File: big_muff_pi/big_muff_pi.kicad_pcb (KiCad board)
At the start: 2 copper layers, 80 x 100 mm, 77 parts, among them J1 Jack_6.35, J2 Jack_6.35, J3 Conn_01x05, J4 Conn_01x05, J5 Conn_01x05, J7 Conn_01x01_Socket, J8 Conn_01x01_Socket, J9 Barrel_Jack_Switch, P1 big_muff_pi_front_panel, Q1 MMBT5551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

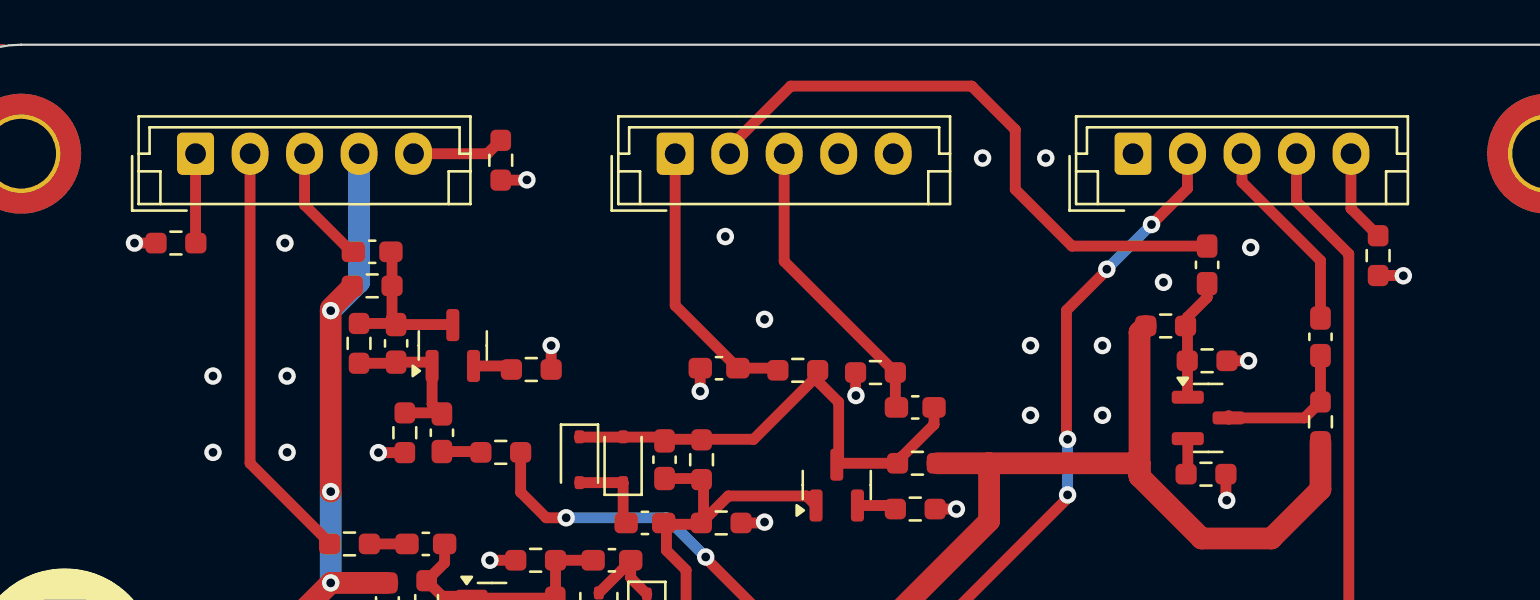
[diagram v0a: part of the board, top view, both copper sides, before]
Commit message: Added IDC, added front plate.
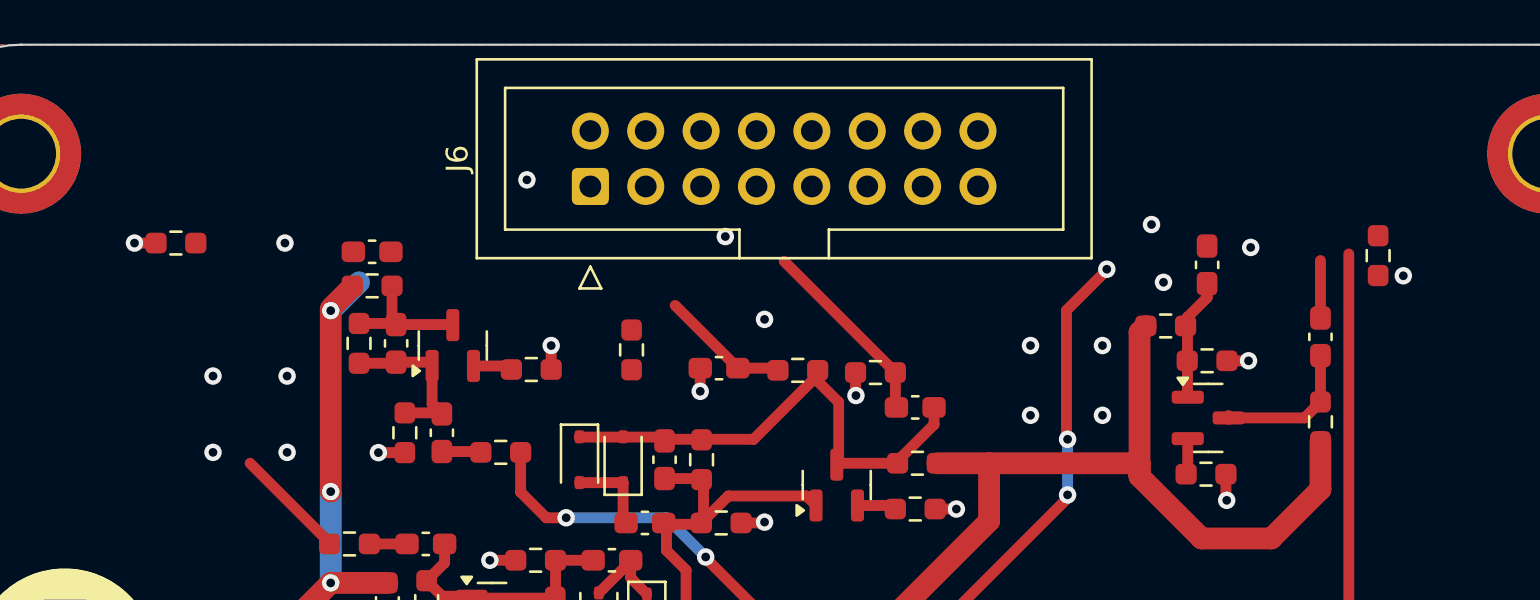
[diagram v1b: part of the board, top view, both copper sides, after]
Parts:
- removed J3, J4, J5: Conn_01x05, Connector_JST:JST_EH_B5B-EH-A_1x05_P2.50mm_Vertical
- added J6: top_panel_connector, Connector_IDC:IDC-Header_2x08_P2.54mm_Vertical, F.Cu at (81.1, 56.5)
- moved R25 10.6 mm to (83.0, 64.0)
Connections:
- R25 pad 1: Net-(J3-Pin_5) -> 9V
- R25 pad 2: 0 -> Net-(J6E-Pin_10)
- R26 pad 2: 0 -> Net-(SW1B-B)
- SW1 pad 5: Net-(J5-Pin_4) -> Net-(SW1B-B)
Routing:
- net Net-(J5-Pin_4): track 100.1 -> 0.00 mm, vias 2 -> 0
- net Net-(SW1B-B): track 0.00 -> 94.5 mm, vias 0 -> 2
- net F_OUT: track 28.0 -> 0.00 mm
- net Net-(J6A-Pin_4): track 19.4 -> 5.21 mm
- net Net-(J6B-Pin_9): track 12.9 -> 5.94 mm
- net Net-(J6C-Pin_14): track 70.5 -> 63.6 mm
- net Net-(J6C-Pin_12): track 9.03 -> 2.64 mm
- net 9V: track 220.5 -> 214.6 mm
- net FS_OUT: track 5.48 -> 0.00 mm
- net Net-(J6B-Pin_5): track 13.8 -> 8.83 mm
- net Net-(J6D-Pin_8): track 4.28 -> 0.00 mm
- net Net-(J3-Pin_5): track 4.25 -> 0.00 mm
- net Net-(J6A-Pin_6): track 4.11 -> 0.00 mm
- net 0: track 18.9 -> 16.5 mm, vias 60 -> 58
- net Net-(Q4-C): track 7.65 -> 6.07 mm

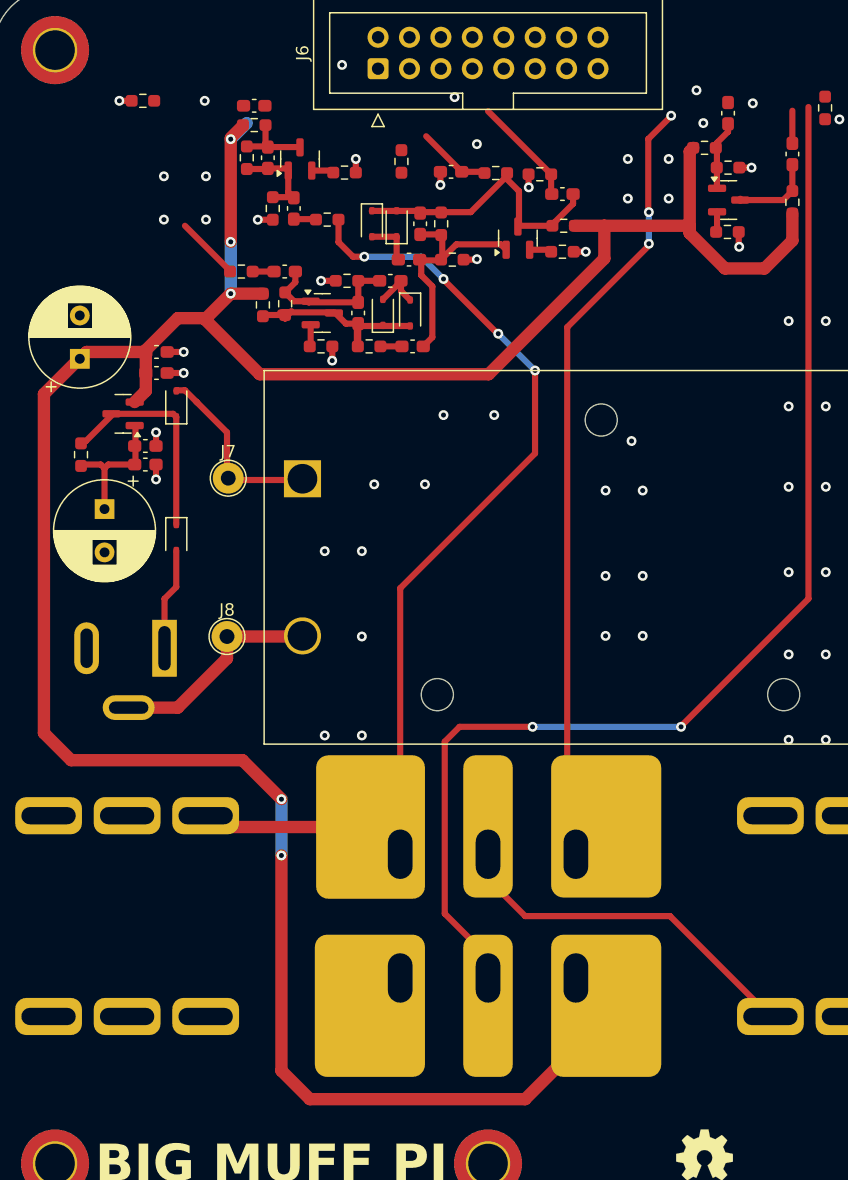
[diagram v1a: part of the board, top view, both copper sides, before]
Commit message: Inputs rotated, power conn moved, spacers updated.
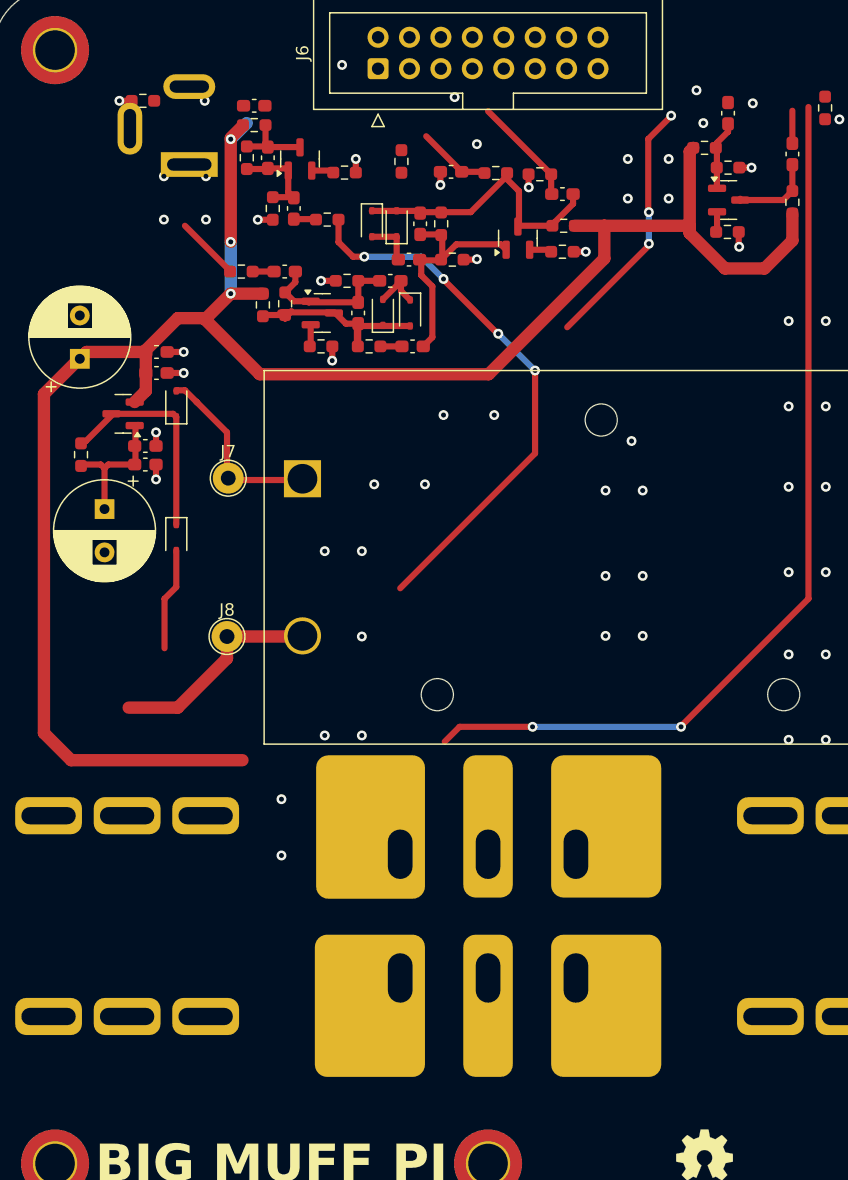
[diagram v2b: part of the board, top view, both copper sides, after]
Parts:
- moved J1 48.4 mm to (112.8, 116.9), turned to 0 degrees
- moved J2 48.4 mm to (67.2, 133.1), turned to 180 degrees
- moved J9 39.2 mm to (65.8, 64.2), turned to 180 degrees
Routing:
- net 9V: track 214.6 -> 156.0 mm
- net Net-(J6C-Pin_14): track 63.6 -> 20.7 mm
- net SW_IN: track 82.7 -> 44.2 mm
- net Net-(SW1A-B): track 29.4 -> 0.00 mm
- net Net-(SW1B-B): track 94.5 -> 74.0 mm

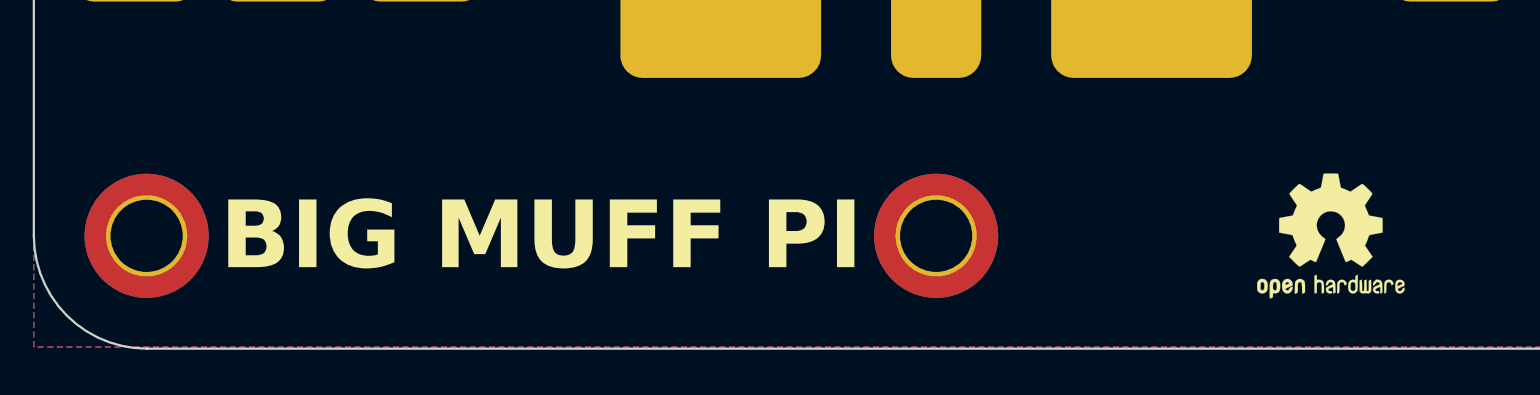
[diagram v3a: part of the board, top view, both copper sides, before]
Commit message: Potentiometers checked, LED updated
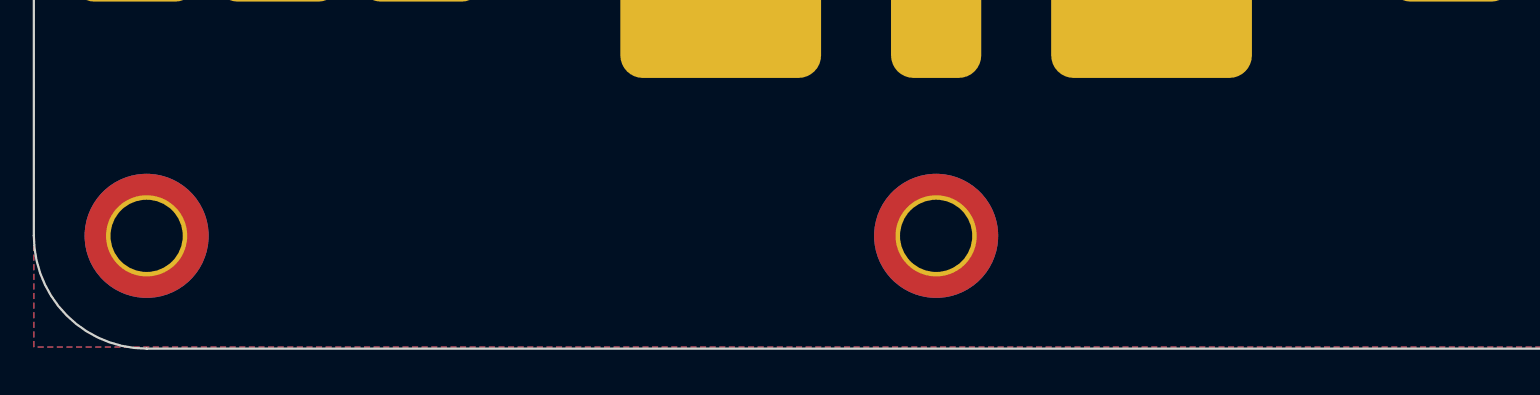
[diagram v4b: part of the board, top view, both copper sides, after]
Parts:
- added REF**: TI logo, pedale:TI logo, B.Cu at (115.5, 145.0)
- SIM1: moved to B.Cu
- moved SIM1 0.25 mm to (107.2, 145.0), turned to 180 degrees
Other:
- board text added: "BMF"
- board text added: "ostojaatanasijevic"
- board text removed: "BIG MUFF PI"

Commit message: small work
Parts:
- removed D4, D7: 1N4148WS, Diode_SMD:D_SOD-323
- removed REF**: TI logo, pedale:TI logo
- added P2: bottom_panel, pedale:bottom_plate, F.Cu at (50.0, 50.0)
- added Q10: AO3401A, Package_TO_SOT_SMD:SOT-23, F.Cu at (60.1, 68.0)
- added Q12: AO3400A, Package_TO_SOT_SMD:SOT-23, F.Cu at (20.5, 72.0)
- added Q13: AO3400A, Package_TO_SOT_SMD:SOT-23, F.Cu at (56.1, 71.5)
- added Q14: AO3400A, Package_TO_SOT_SMD:SOT-23, F.Cu at (56.1, 68.0)
- added Q6: AO3401A, Package_TO_SOT_SMD:SOT-23, F.Cu at (20.5, 58.1)
- added Q8: AO3401A, Package_TO_SOT_SMD:SOT-23, F.Cu at (60.1, 71.5)
- added R23: 100k, Resistor_SMD:R_0603_1608Metric_Pad0.98x0.95mm_HandSolder, F.Cu at (25.1, 57.0)
- added R27: 100k, Resistor_SMD:R_0603_1608Metric_Pad0.98x0.95mm_HandSolder, F.Cu at (25.1, 59.5)
- moved C14 77.6 mm to (-11.2, 112.0)
- moved C16 77.6 mm to (-10.3, 106.1)
- moved C17 77.6 mm to (-10.3, 104.4)
- moved C18 77.6 mm to (-11.2, 113.5)
- moved C19 77.6 mm to (-16.5, 105.0)
- moved C20 77.6 mm to (-14.5, 117.1)
- moved Q5 77.6 mm to (-13.0, 109.4)
- moved R24 77.6 mm to (-16.4, 112.7)
- moved R6 14.0 mm to (73.8, 51.5)
- moved BT1 4.45 mm to (75.0, 94.1)
- moved J7 4.40 mm to (69.0, 94.0)
- moved J8 4.40 mm to (68.9, 106.8)
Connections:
- net Net-(BT1-+) renamed BAT+
- net Net-(BT1--) renamed BAT-
- net Net-(D4-K) renamed REG_IN
- J1 pad SN: unconnected-(J1-PadSN) -> IN_CONNECT
- J9 pad 1: Net-(D7-A) -> CONN+
- J9 pad 2: 0 -> CONN-
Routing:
- net Net-(SW1B-B): track 74.0 -> 0.00 mm
- net 9V: track 156.0 -> 111.7 mm
- net CONN-: track 0.00 -> 26.5 mm, vias 0 -> 2
- net SW_IN: track 44.2 -> 22.0 mm
- net BAT-: track 17.5 -> 0.00 mm
- net CONN+: track 0.00 -> 10.6 mm, vias 0 -> 1
- net REG_IN: track 17.3 -> 26.9 mm
- net Net-(D7-A): track 8.29 -> 0.00 mm
- net 0: track 16.5 -> 19.4 mm, vias 58 -> 57
